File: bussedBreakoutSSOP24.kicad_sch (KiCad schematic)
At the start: 49 parts, among them J1 Conn_01x12_Pin, J10 Conn_01x06_Pin, J11 Conn_01x06_Pin, J12 Conn_01x06_Pin, J13 Conn_01x06_Pin, J14 Conn_01x06_Pin, J15 Conn_01x06_Pin, J16 Conn_01x06_Pin, J17 Conn_01x06_Pin, J18 Conn_01x06_Pin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

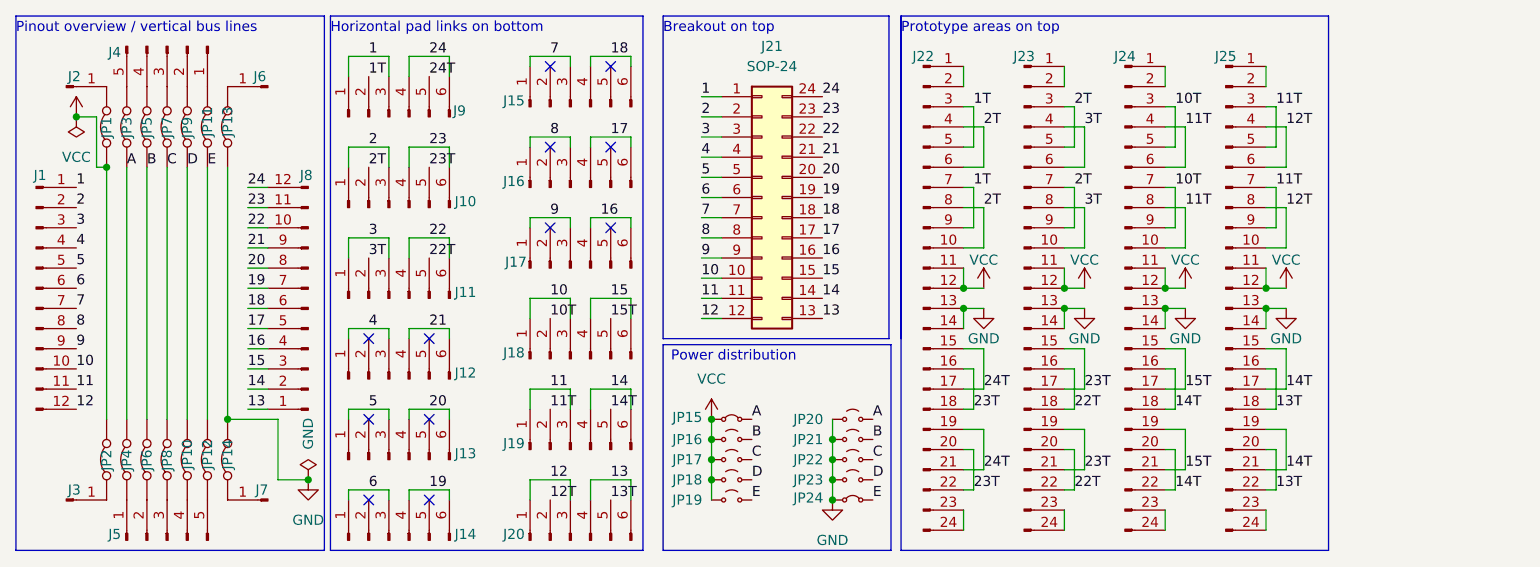
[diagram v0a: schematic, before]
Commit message: Change to SSOP24 breakout
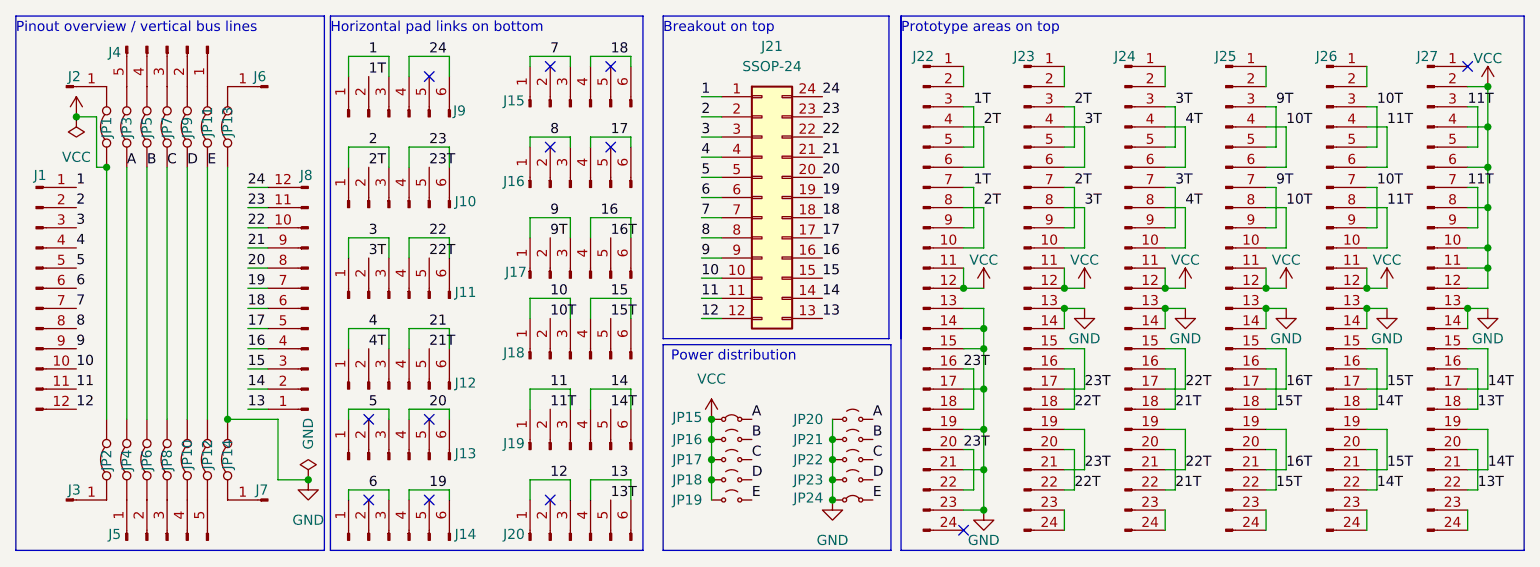
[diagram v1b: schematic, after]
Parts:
- added J26, J27: Conn_01x24_Pin, SMD:SMD_grid_2x12_0402, symbol Connector:Conn_01x24_Pin
- J21: value SOP-24 -> SSOP-24; footprint SMD:SOP-24_3.9-7.5mmx15.4mm_P1.27mm -> SMD:SSOP-24_3.9-7.5mmx8.2mm_P0.65mm
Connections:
- net 10T: now also J25.10 (Pin_10), J25.4 (Pin_4), J25.6 (Pin_6), J25.8 (Pin_8), J26.3 (Pin_3), J26.5 (Pin_5), J26.7 (Pin_7), J26.9 (Pin_9); no longer J24.3 (Pin_3), J24.5 (Pin_5), J24.7 (Pin_7), J24.9 (Pin_9)
- net 11T: now also J26.10 (Pin_10), J26.4 (Pin_4), J26.6 (Pin_6), J26.8 (Pin_8), J27.3 (Pin_3), J27.5 (Pin_5), J27.7 (Pin_7), J27.9 (Pin_9); no longer J24.10 (Pin_10), J24.4 (Pin_4), J24.6 (Pin_6), J24.8 (Pin_8), J25.3 (Pin_3), J25.5 (Pin_5), J25.7 (Pin_7), J25.9 (Pin_9)
- net 13T: now also J27.16 (Pin_16), J27.18 (Pin_18), J27.20 (Pin_20), J27.22 (Pin_22); no longer J25.16 (Pin_16), J25.18 (Pin_18), J25.20 (Pin_20), J25.22 (Pin_22)
- net 14T: now also J26.16 (Pin_16), J26.18 (Pin_18), J26.20 (Pin_20), J26.22 (Pin_22), J27.15 (Pin_15), J27.17 (Pin_17), J27.19 (Pin_19), J27.21 (Pin_21); no longer J24.16 (Pin_16), J24.18 (Pin_18), J24.20 (Pin_20), J24.22 (Pin_22), J25.15 (Pin_15), J25.17 (Pin_17), J25.19 (Pin_19), J25.21 (Pin_21)
- net 15T: now also J25.16 (Pin_16), J25.18 (Pin_18), J25.20 (Pin_20), J25.22 (Pin_22), J26.15 (Pin_15), J26.17 (Pin_17), J26.19 (Pin_19), J26.21 (Pin_21); no longer J24.15 (Pin_15), J24.17 (Pin_17), J24.19 (Pin_19), J24.21 (Pin_21)
- net 22T: now also J24.15 (Pin_15), J24.17 (Pin_17), J24.19 (Pin_19), J24.21 (Pin_21)
- net 3T: now also J24.3 (Pin_3), J24.5 (Pin_5), J24.7 (Pin_7), J24.9 (Pin_9)
- net GND: now also J22.15 (Pin_15), J22.17 (Pin_17), J22.19 (Pin_19), J22.21 (Pin_21), J22.23 (Pin_23), J26.13 (Pin_13), J26.14 (Pin_14), J27.13 (Pin_13), J27.14 (Pin_14)
- net VCC: now also J26.11 (Pin_11), J26.12 (Pin_12), J27.10 (Pin_10), J27.11 (Pin_11), J27.12 (Pin_12), J27.2 (Pin_2), J27.4 (Pin_4), J27.6 (Pin_6), J27.8 (Pin_8)
- net 9T: now reaches J17.2 (Pin_2)
- net 9T: now also J25.3 (Pin_3), J25.5 (Pin_5), J25.7 (Pin_7), J25.9 (Pin_9)
- net 16T: now reaches J17.5 (Pin_5)
- net 16T: now also J25.15 (Pin_15), J25.17 (Pin_17), J25.19 (Pin_19), J25.21 (Pin_21)
- net at J22.24 (Pin_24): no longer J22.23 (Pin_23)
- net 4T: now reaches J12.2 (Pin_2)
- net 4T: now also J24.10 (Pin_10), J24.4 (Pin_4), J24.6 (Pin_6), J24.8 (Pin_8)
- net 21T: now reaches J12.5 (Pin_5)
- net 21T: now also J24.16 (Pin_16), J24.18 (Pin_18), J24.20 (Pin_20), J24.22 (Pin_22)
- removed net 12T: J20.2 (Pin_2), J25.10 (Pin_10), J25.4 (Pin_4), J25.6 (Pin_6), J25.8 (Pin_8)
- removed net 24T: J22.15 (Pin_15), J22.17 (Pin_17), J22.19 (Pin_19), J22.21 (Pin_21), J9.5 (Pin_5)
- new net: J27.23 (Pin_23), J27.24 (Pin_24)
- new net: J26.1 (Pin_1), J26.2 (Pin_2)
- new net: J26.23 (Pin_23), J26.24 (Pin_24)
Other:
- moved on the sheet: J12, J17

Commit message: Reorient power distribution jumpers to remove GND/VCC routing workaround
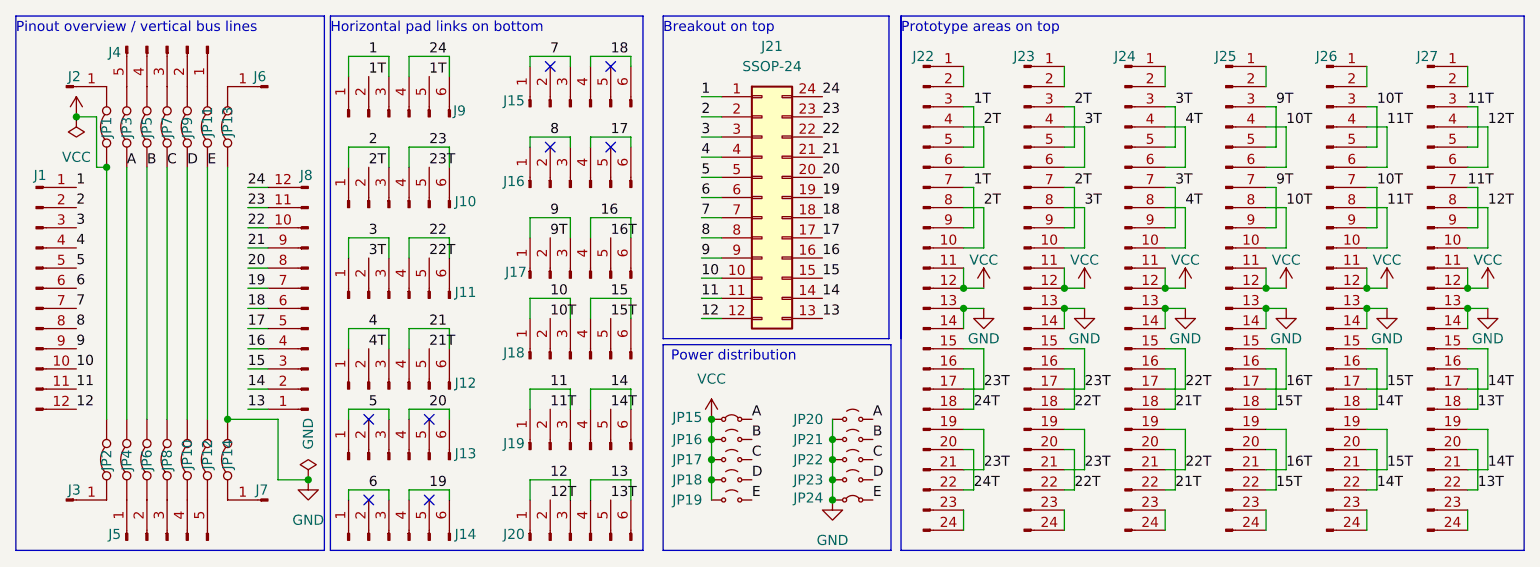
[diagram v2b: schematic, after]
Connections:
- net 1T: now also J9.5 (Pin_5)
- net 23T: now also J22.15 (Pin_15), J22.17 (Pin_17), J22.19 (Pin_19), J22.21 (Pin_21); no longer J22.16 (Pin_16), J22.18 (Pin_18), J22.20 (Pin_20), J22.22 (Pin_22)
- net GND: no longer J22.15 (Pin_15), J22.17 (Pin_17), J22.19 (Pin_19), J22.21 (Pin_21), J22.23 (Pin_23)
- net VCC: no longer J27.10 (Pin_10), J27.2 (Pin_2), J27.4 (Pin_4), J27.6 (Pin_6), J27.8 (Pin_8)
- net at J22.24 (Pin_24): now also J22.23 (Pin_23)
- net at J27.1 (Pin_1): now also J27.2 (Pin_2)
- net 12T: now reaches J20.2 (Pin_2)
- net 12T: now also J27.10 (Pin_10), J27.4 (Pin_4), J27.6 (Pin_6), J27.8 (Pin_8)
- new net 24T: J22.16 (Pin_16), J22.18 (Pin_18), J22.20 (Pin_20), J22.22 (Pin_22)
- no-connect marks 12 -> 8

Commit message: Fix missing T24/T23 vias
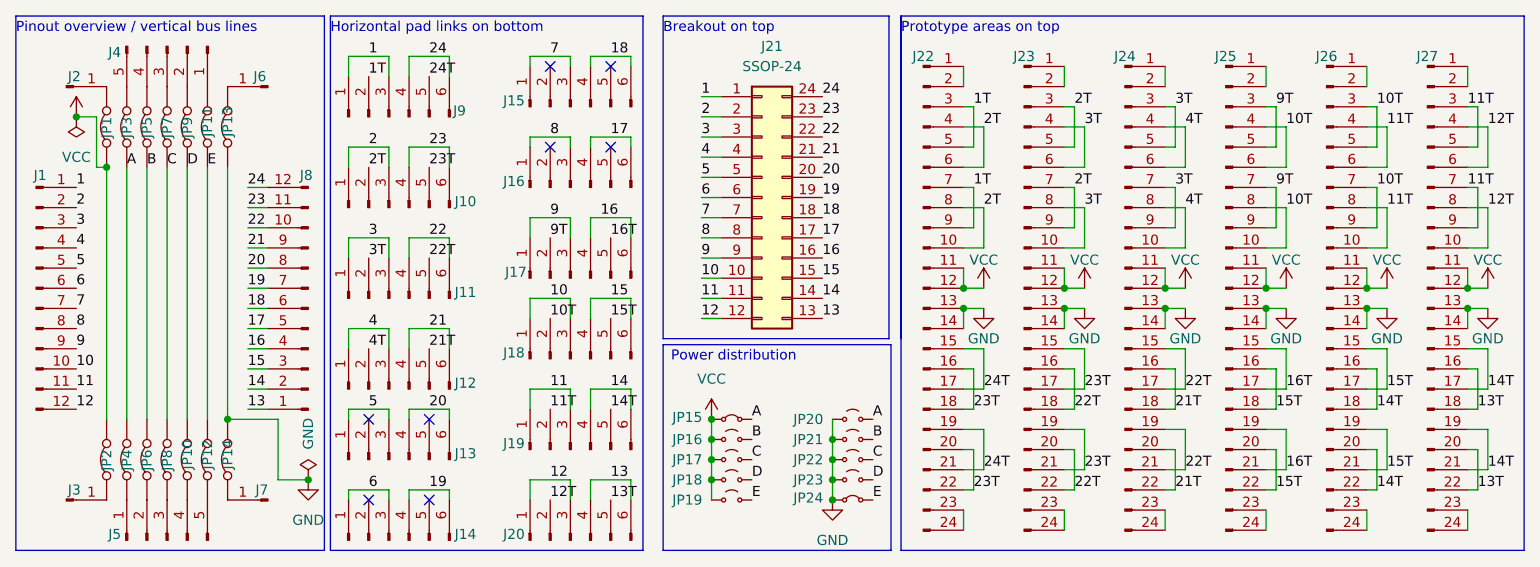
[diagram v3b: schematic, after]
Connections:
- net 1T: no longer J9.5 (Pin_5)
- net 23T: now also J22.16 (Pin_16), J22.18 (Pin_18), J22.20 (Pin_20), J22.22 (Pin_22); no longer J22.15 (Pin_15), J22.17 (Pin_17), J22.19 (Pin_19), J22.21 (Pin_21)
- net 24T: now also J22.15 (Pin_15), J22.17 (Pin_17), J22.19 (Pin_19), J22.21 (Pin_21), J9.5 (Pin_5); no longer J22.16 (Pin_16), J22.18 (Pin_18), J22.20 (Pin_20), J22.22 (Pin_22)
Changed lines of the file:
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@@
 		)
 	)
-	(label "23T"
+	(label "24T"
 		(at 134.62 69.85 0)
 		(effects
@@
 		)
 	)
-	(label "1T"
+	(label "24T"
 		(at 64.77 20.32 0)
 		(effects
@@
 		)
 	)
-	(label "24T"
+	(label "23T"
 		(at 133.35 72.39 0)
 		(effects
@@
 		)
 	)
-	(label "24T"
+	(label "23T"
 		(at 133.35 62.23 0)
 		(effects
@@
 		)
 	)
-	(label "23T"
+	(label "24T"
 		(at 134.62 59.69 0)
 		(effects

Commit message: Fix/exclude DRC errors
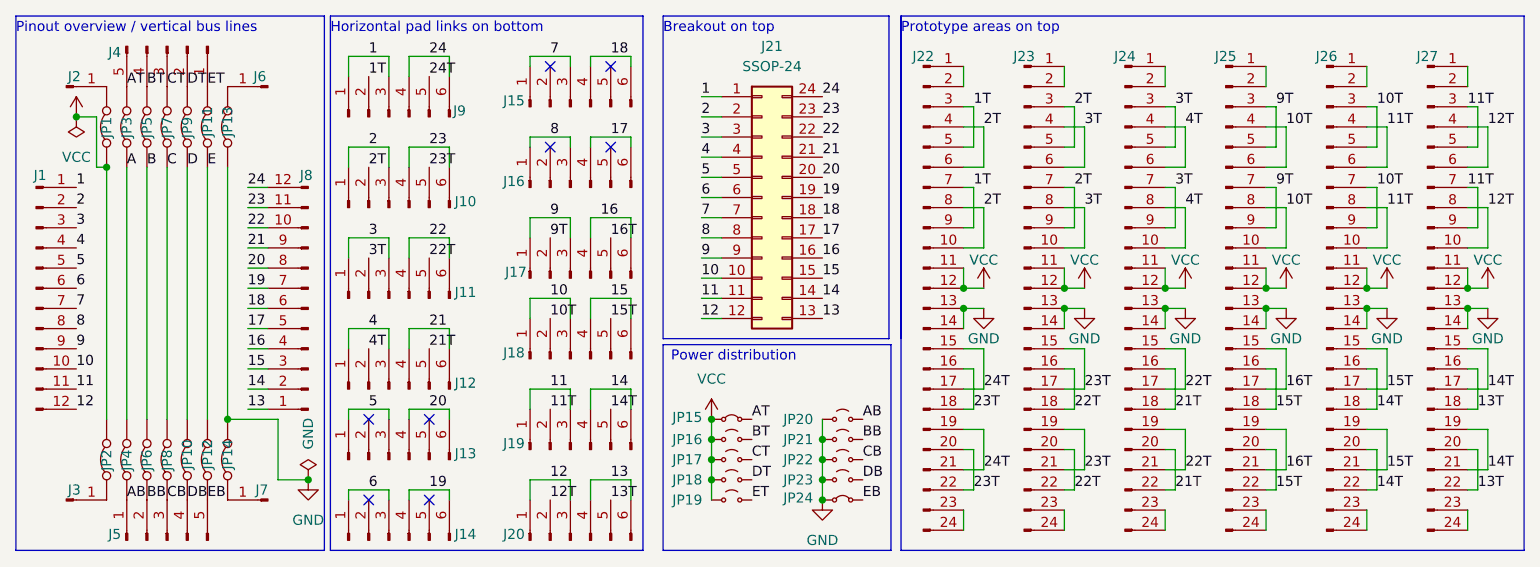
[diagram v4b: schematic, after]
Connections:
- net A: no longer JP15.2 (B), JP20.2 (B)
- net B: no longer JP16.2 (B), JP21.2 (B)
- net C: no longer JP17.2 (B), JP22.2 (B)
- net D: no longer JP18.2 (B), JP23.2 (B)
- net E: no longer JP19.2 (B), JP24.2 (B)
- net BB: now reaches J5.2 (Pin_2), JP6.1 (A)
- net BB: now also JP21.2 (B)
- net BT: now reaches J4.4 (Pin_4), JP5.2 (B)
- net BT: now also JP16.2 (B)
- net AB: now reaches J5.1 (Pin_1), JP4.1 (A)
- net AB: now also JP20.2 (B)
- net CB: now reaches J5.3 (Pin_3), JP8.1 (A)
- net CB: now also JP22.2 (B)
- net DB: now reaches J5.4 (Pin_4), JP10.1 (A)
- net DB: now also JP23.2 (B)
- net EB: now reaches J5.5 (Pin_5), JP12.1 (A)
- net EB: now also JP24.2 (B)
- net ET: now reaches J4.1 (Pin_1), JP11.2 (B)
- net ET: now also JP19.2 (B)
- net DT: now reaches J4.2 (Pin_2), JP9.2 (B)
- net DT: now also JP18.2 (B)
- net CT: now reaches J4.3 (Pin_3), JP7.2 (B)
- net CT: now also JP17.2 (B)
- net AT: now reaches J4.5 (Pin_5), JP3.2 (B)
- net AT: now also JP15.2 (B)
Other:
- moved on the sheet: JP20, JP21, JP22, JP23, JP24
